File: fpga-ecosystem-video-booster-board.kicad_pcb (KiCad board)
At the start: 4 copper layers, 26.9 x 20.3 mm, 50 parts, among them J1 0473460001, J2 HDMI-PE10-19-LF, J3 61300411121, J4 M20-9990246, J5 M20-9990246, J6 685119134923_, U1 LP2985-33DBVR, U2 EFM32HG309, U3 PTN3363

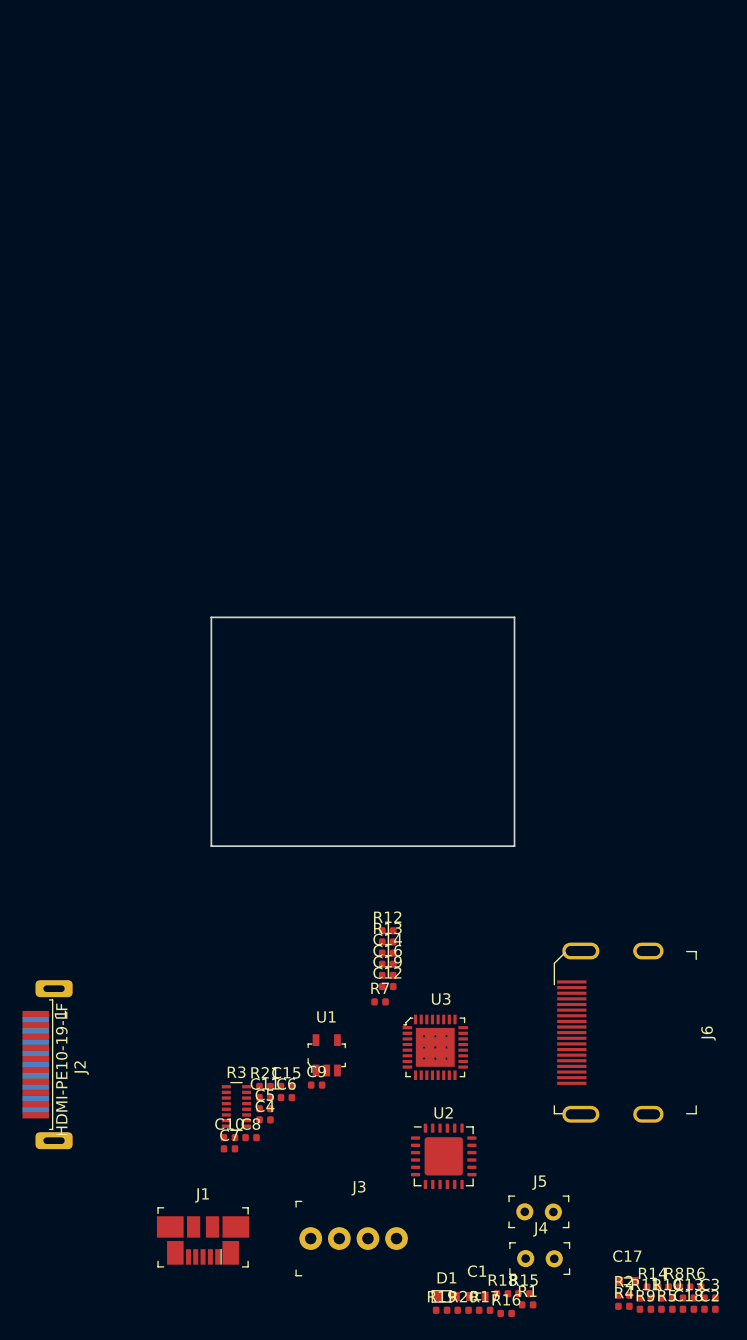
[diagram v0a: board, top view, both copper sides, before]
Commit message: Board shape, initial component layout
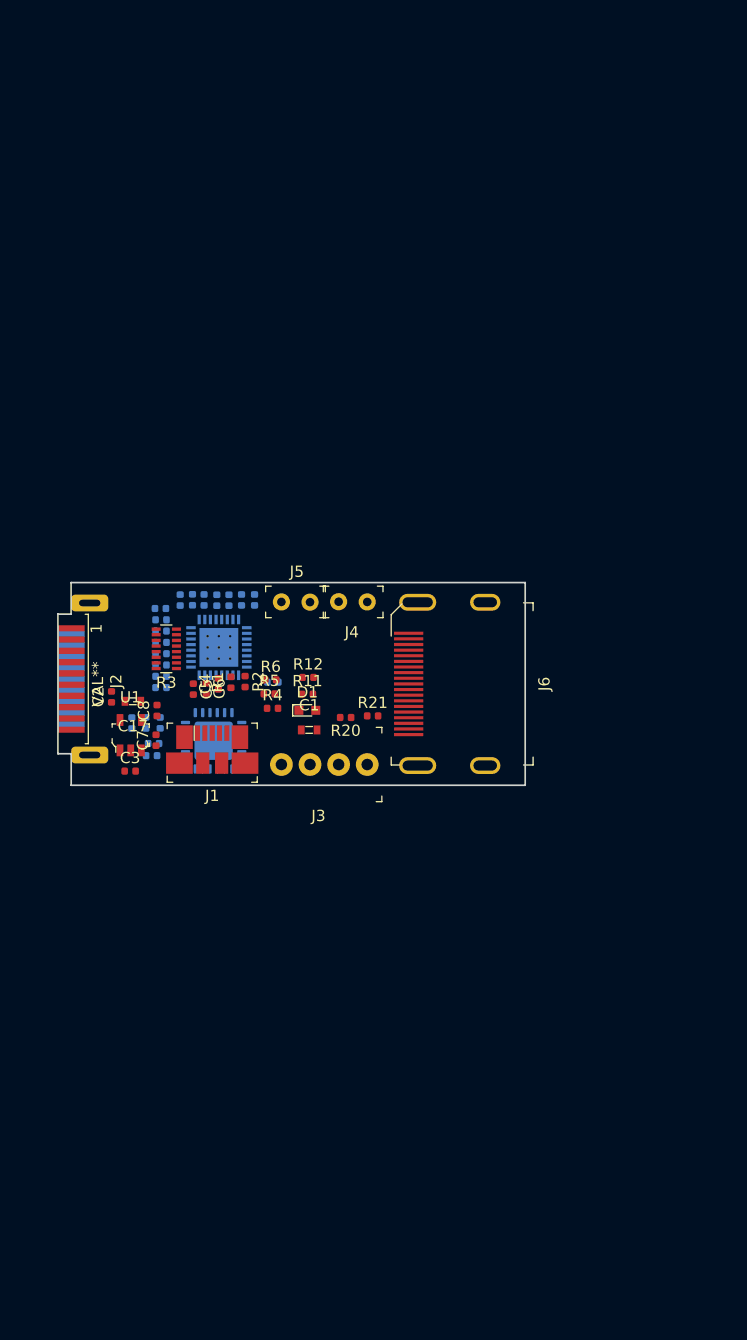
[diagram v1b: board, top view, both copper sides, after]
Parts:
- C10, C11, C12, C13, C14, C15, C16, C18, C19, C9, R10, R13, R14, R15, R16, R17, R18, R19, R7, R8, R9, U2, U3: moved to B.Cu
- J2: value HDMI-PE10-19-LF -> VAL**
- moved C18 77.5 mm to (124.4, 83.6), turned to 270 degrees
- moved C13 77.1 mm to (122.6, 84.3), turned to 180 degrees
- moved C2 76.0 mm to (118.3, 92.2), turned to 90 degrees
- moved R8 74.5 mm to (125.5, 83.5), turned to 270 degrees
- moved C3 69.6 mm to (119.9, 98.7)
- moved R15 67.8 mm to (126.5, 83.5), turned to 270 degrees
- moved C17 67.7 mm to (120.2, 92.5), turned to 180 degrees
- moved R10 67.1 mm to (122.0, 96.3)
- moved R14 66.5 mm to (122.6, 94.5), turned to 90 degrees
- moved R18 66.2 mm to (128.7, 83.6), turned to 270 degrees
- moved R9 65.9 mm to (121.8, 97.4)
- moved R6 65.8 mm to (132.4, 90.6)
- moved R19 65.5 mm to (129.8, 83.5), turned to 270 degrees
- moved R5 65.1 mm to (132.3, 91.9)
- moved R2 64.0 mm to (130.1, 90.8), turned to 270 degrees
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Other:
- board size 26.9 x 20.3 mm -> 41.5 x 18 mm

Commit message: New board shape, initial placement
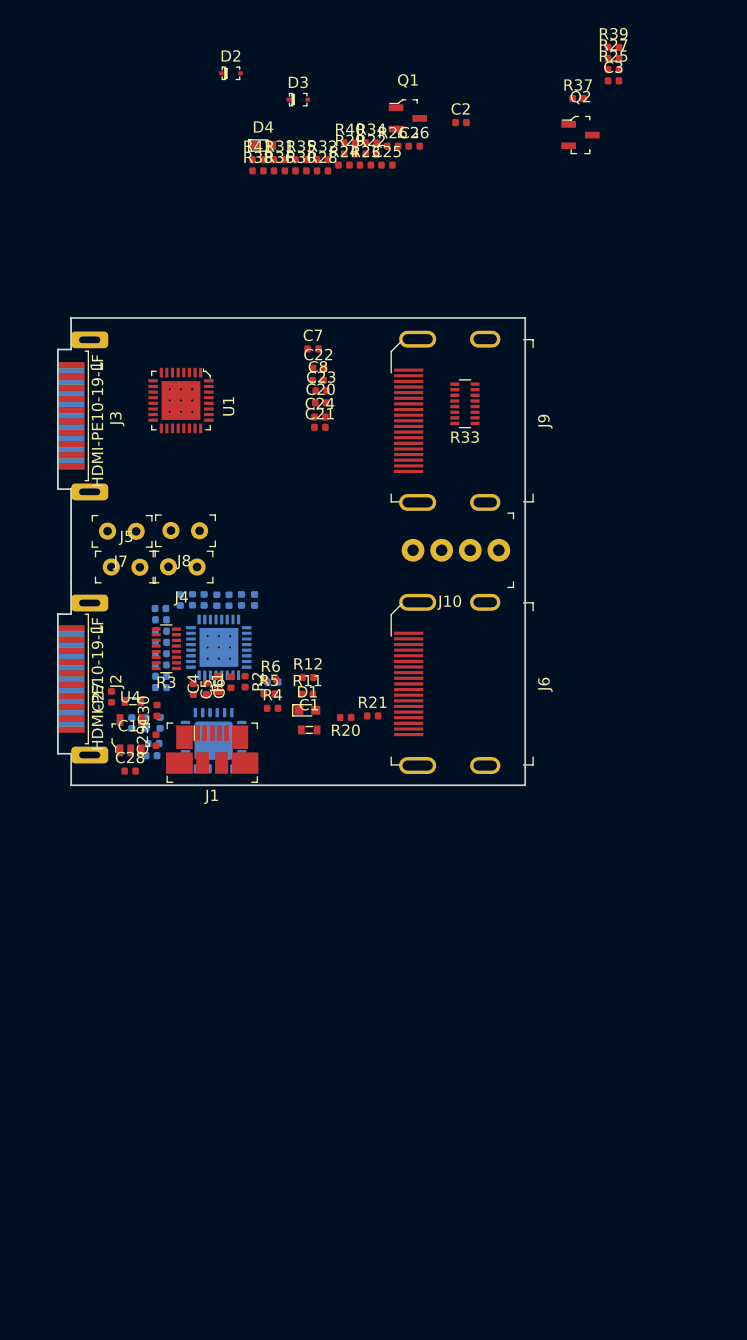
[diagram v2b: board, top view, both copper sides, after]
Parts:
- added C2: C_100n_0402_6V3, antmicro-footprints:0402-cap, F.Cu at (149.3, 41.1)
- added C20: C_100n_0402_6V3, antmicro-footprints:0402-cap, F.Cu at (136.8, 66.0)
- added C21: C_100n_0402_6V3, antmicro-footprints:0402-cap, F.Cu at (136.8, 68.2)
- added C22: C_100n_0402_6V3, antmicro-footprints:0402-cap, F.Cu at (136.6, 63.0)
- added C23: C_100n_0402_6V3, antmicro-footprints:0402-cap, F.Cu at (136.9, 65.0)
- added C24: C_100n_0402_6V3, antmicro-footprints:0402-cap, F.Cu at (136.8, 67.3)
- added C25: C_100n_0402_6V3, antmicro-footprints:0402-cap, F.Cu at (142.7, 44.9)
- added C26: C_1u_0402, antmicro-footprints:0402-cap, F.Cu at (145.1, 43.2)
- added C3: C_100n_0402_6V3, antmicro-footprints:0402-cap, F.Cu at (162.8, 37.4)
- added C7: C_100n_0402_6V3, antmicro-footprints:0402-cap, F.Cu at (136.2, 61.2)
- added C8: C_100n_0402_6V3, antmicro-footprints:0402-cap, F.Cu at (136.6, 64.0)
- added D2: BAT54-02V-V-G, antmicro-footprints:SOD-523, F.Cu at (128.9, 36.8)
- added D3: BAT54-02V-V-G, antmicro-footprints:SOD-523, F.Cu at (134.8, 39.1)
- added D4: LG_L29K-G2J1-24-Z, antmicro-footprints:LED_0603, F.Cu at (131.7, 43.2)
- added J3: HDMI-PE10-19-LF, antmicro-footprints:HDMI-PE10-19-LF, F.Cu at (114.7, 67.2)
- added J7: M20-9990246, antmicro-footprints:PinHeader_1x2_P2.54mm, F.Cu at (120.5, 77.5)
- added J8: M20-9990246, antmicro-footprints:PinHeader_1x2_P2.54mm, F.Cu at (126.1, 77.4)
- added J9: 685119134923_, antmicro-footprints:HDMI_A_Female_685119134923, F.Cu at (145.9, 67.6)
- added Q1: BSS138-7-F, antmicro-footprints:SOT-23-3, F.Cu at (144.6, 40.8)
- added Q2: BSS138-7-F, antmicro-footprints:SOT-23-3, F.Cu at (159.9, 42.3)
- added R22: R_10k_0402, antmicro-footprints:0402-res, F.Cu at (141.3, 43.9)
- added R23: R_10k_0402, antmicro-footprints:0402-res, F.Cu at (140.8, 44.9)
- added R24: R_100k_0402, antmicro-footprints:0402-res, F.Cu at (138.9, 44.9)
- added R25: R_100k_0402, antmicro-footprints:0402-res, F.Cu at (162.8, 36.4)
- added R26: R_10k_0402, antmicro-footprints:0402-res, F.Cu at (143.2, 43.2)
- added R27: R_10k_0402, antmicro-footprints:0402-res, F.Cu at (162.8, 35.5)
- added R28: R_10k_0402, antmicro-footprints:0402-res, F.Cu at (137.0, 45.4)
- added R29: R_10k_0402, antmicro-footprints:0402-res, F.Cu at (139.4, 43.9)
- added R30: R_10k_0402, antmicro-footprints:0402-res, F.Cu at (135.1, 45.4)
- added R31: R_10k_0402, antmicro-footprints:0402-res, F.Cu at (133.2, 44.4)
- added R32: R_10k_0402, antmicro-footprints:0402-res, F.Cu at (137.0, 44.4)
- added R33: 8x51R_0602_array, antmicro-footprints:R_Array_Convex_8x0602, F.Cu at (149.7, 66.1)
- added R34: R_10k_0402, antmicro-footprints:0402-res, F.Cu at (141.3, 42.9)
- added R35: R_10k_0402, antmicro-footprints:0402-res, F.Cu at (135.1, 44.4)
- added R36: R_10k_0402, antmicro-footprints:0402-res, F.Cu at (133.2, 45.4)
- added R37: R_10k_0402, antmicro-footprints:0402-res, F.Cu at (159.7, 39.0)
- added R38: R_10k_0402, antmicro-footprints:0402-res, F.Cu at (131.3, 45.4)
- added R39: R_10k_0402, antmicro-footprints:0402-res, F.Cu at (162.8, 34.5)
- added R40: R_10k_0402, antmicro-footprints:0402-res, F.Cu at (139.4, 42.9)
- added R41: R_330R_0402, antmicro-footprints:0402-res, F.Cu at (131.3, 44.4)
- added U1: PTN3363, antmicro-footprints:QFN-32-1EP_5x5mm, F.Cu at (124.0, 66.3)
- C4: value C_1u_0402 -> C_10u_0603; footprint antmicro-footprints:0402-cap -> antmicro-footprints:0603-cap
- J2: value VAL** -> HDMI-PE10-19-LF
- R11, R12: value R_15R_0402 -> R_0R_0402
- R14, R15, R5, R6: value R_10k_0402 -> R_100k_0402
- R17: value R_10k_0402 -> R_12k4_0402
- R18, R21: value R_4k7_0402 -> R_10k_0402
- R19, R20: value R_4k7_0402 -> R_100k_0402
- R7, R8: value R_100k_0402 -> R_0R_0402
- moved J10 22.3 mm to (152.7, 79.1)
- moved J4 15.4 mm to (125.9, 80.6)
- moved J5 15.4 mm to (118.2, 80.6)
- renumbered C2 to C27, C3 to C28, C7 to C29, C8 to C30, J3 to J10, U1 to U4
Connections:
- net /CEC renamed /TX_CEC
- net /C_IN_CLK_N renamed /C_TX_IN_CLK_N
- net /C_IN_CLK_P renamed /C_TX_IN_CLK_P
- net /C_IN_D0_N renamed /C_TX_IN_D0_N
- net /C_IN_D0_P renamed /C_TX_IN_D0_P
- net /C_IN_D1_N renamed /C_TX_IN_D1_N
- net /C_IN_D1_P renamed /C_TX_IN_D1_P
- net /C_IN_D2_N renamed /C_TX_IN_D2_N
- net /C_IN_D2_P renamed /C_TX_IN_D2_P
- net /IN_CLK_P renamed /TX_IN_CLK_P
- net /IN_D0_N renamed /TX_IN_D0_N
- net /IN_D0_P renamed /TX_IN_D0_P
- net /IN_D1_N renamed /TX_IN_D1_N
- net /IN_D1_P renamed /TX_IN_D1_P
- net /IN_D2_N renamed /TX_IN_D2_N
- net /IN_D2_P renamed /TX_IN_D2_P
- net /OUT_CLK_N renamed /TX_OUT_CLK_N
- net /OUT_CLK_P renamed /TX_OUT_CLK_P
- net /OUT_D0_N renamed /TX_OUT_D0_N
- net /OUT_D0_P renamed /TX_OUT_D0_P
- net /OUT_D1_N renamed /TX_OUT_D1_N
- net /OUT_D1_P renamed /TX_OUT_D1_P
- net /OUT_D2_N renamed /TX_OUT_D2_N
- net /OUT_D2_P renamed /TX_OUT_D2_P
- net /UTILITY renamed /TX_UTILITY
- C12 pad 2: /IN_CLK_N -> Net-(C12-Pad2)
- C4 pad 1: Net-(C4-Pad1) -> VDD
- J2 pad 12: /IN_CLK_N -> /TX_IN_CLK_N
- J2 pad 15: /SCL_SRC -> Net-(J2-Pad15)
- J2 pad 16: /SDA_SRC -> Net-(J2-Pad16)
- J2 pad 18: +5V -> /TX_5V
- J2 pad 19: /HPD_SRC -> /TX_HPD
- J4 pad 1: /EQ0 -> /TX_EQ0
- J5 pad 1: /EQ1 -> /TX_EQ1
- J6 pad 15: /SCL_SINK -> /TX_SCL
- J6 pad 16: /SDA_SINK -> /TX_SDA
- J6 pad 18: +5V -> /TX_5V
- J6 pad 19: /HPD_SINK -> /TX_HPD
- R10 pad 1: /DBG_SWDIO -> /TX_EQ1
- R10 pad 2: /UART_RX -> Net-(R10-Pad2)
- R11 pad 1: /SCL_MCU -> Net-(J3-Pad15)
- R11 pad 2: /SCL_SRC -> /TX_SDA
- R12 pad 1: /SDA_MCU -> Net-(J3-Pad16)
- R12 pad 2: /SDA_SRC -> /TX_SCL
- R14 pad 2: /DCC_EN -> /RX_EQ0
- R15 pad 2: /DDET -> /RX_EQ1
- R16 pad 1: VDD -> GND
- R16 pad 2: /HIZ_EN -> /RX_5V
- R17 pad 1: /HIZ_EN -> GND
- R17 pad 2: GND -> Net-(R17-Pad2)
- R18 pad 1: VDD -> Net-(Q1-Pad3)
- R18 pad 2: /SDA_SRC -> VDD
- R19 pad 2: /SCL_SRC -> /TX_DCC_EN
- R20 pad 1: +5V -> /TX_DCC_EN
- R20 pad 2: /SDA_SINK -> GND
- R21 pad 1: +5V -> VDD
- R21 pad 2: /SCL_SINK -> /TX_DDET
- R3 pad 16: /IN_CLK_N -> Net-(C12-Pad2)
- R5 pad 1: /EQ0 -> VDD
- R5 pad 2: Net-(R5-Pad2) -> /TX_EQ0
- R6 pad 1: /EQ1 -> VDD
- R6 pad 2: Net-(R6-Pad2) -> /TX_EQ1
- R7 pad 1: VDD -> Net-(J2-Pad15)
- R7 pad 2: /EQ0 -> /TX_SDA
- R8 pad 1: VDD -> Net-(J2-Pad16)
- R8 pad 2: /EQ1 -> /TX_SCL
- R9 pad 1: /DBG_SWCLK -> /TX_EQ0
- R9 pad 2: /UART_TX -> Net-(R9-Pad2)
- U2 pad 10: /UART_TX -> /TX_HIZ_EN
- U2 pad 11: /UART_RX -> /RX_HIZ_EN
- U2 pad 16: Net-(C4-Pad1) -> Net-(C26-Pad1)
- U2 pad 21: (no net) -> Net-(R41-Pad1)
- U2 pad 23: /SDA_MCU -> /MCU_SDA
- U2 pad 24: /SCL_MCU -> /MCU_SCL
- U2 pad 3: /DDET -> Net-(R39-Pad2)
- U2 pad 4: /DCC_EN -> Net-(R40-Pad2)
- U2 pad 5: Net-(R5-Pad2) -> Net-(R9-Pad2)
- U2 pad 6: Net-(R6-Pad2) -> Net-(R10-Pad2)
- U2 pad 8: /HIZ_EN -> Net-(R38-Pad2)
- U3 pad 17: GND -> Net-(Q2-Pad3)
- U3 pad 19: /SCL_SINK -> /TX_SDA
- U3 pad 2: /EQ1 -> /TX_EQ1
- U3 pad 20: /SDA_SINK -> /TX_SCl
- U3 pad 21: /HPD_SINK -> Net-(U3-Pad21)
- U3 pad 22: /DCC_EN -> /TX_DCC_EN
- U3 pad 24: /HIZ_EN -> /TX_HIZ_EN
- U3 pad 3: /DDET -> /TX_DDET
- U3 pad 5: /HPD_SRC -> Net-(U3-Pad5)
- U3 pad 6: /SDA_SRC -> /MCU_SDA
- U3 pad 7: /SCL_SRC -> /MCU_SCL
- U3 pad 8: /EQ0 -> /TX_EQ0
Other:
- board size 41.5 x 18 mm -> 41.5 x 41.5 mm

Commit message: Channels flipped for 1-side component placement
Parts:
- added R42: R_49R9_0402, antmicro-footprints:0402-res, F.Cu at (118.3, 88.4)
- added R43: R_49R9_0402, antmicro-footprints:0402-res, F.Cu at (118.3, 87.4)
- added R44: R_49R9_0402, antmicro-footprints:0402-res, F.Cu at (118.3, 90.4)
- added R45: R_49R9_0402, antmicro-footprints:0402-res, F.Cu at (118.3, 89.4)
- added R46: R_49R9_0402, antmicro-footprints:0402-res, F.Cu at (118.3, 92.4)
- added R47: R_49R9_0402, antmicro-footprints:0402-res, F.Cu at (118.3, 91.4)
- added R48: R_49R9_0402, antmicro-footprints:0402-res, F.Cu at (131.0, 69.5)
- added R49: R_49R9_0402, antmicro-footprints:0402-res, F.Cu at (132.0, 67.9)
- added R50: R_49R9_0402, antmicro-footprints:0402-res, F.Cu at (130.0, 67.4)
- added R51: R_49R9_0402, antmicro-footprints:0402-res, F.Cu at (130.1, 65.9)
- added R52: R_49R9_0402, antmicro-footprints:0402-res, F.Cu at (132.0, 65.4)
- added R53: R_49R9_0402, antmicro-footprints:0402-res, F.Cu at (132.0, 63.8)
- added R54: R_49R9_0402, antmicro-footprints:0402-res, F.Cu at (130.0, 63.4)
- added R55: R_49R9_0402, antmicro-footprints:0402-res, F.Cu at (130.0, 61.8)
- C10, C11, C12, C13, C14, C15, C16, C18, C9, R10, R13, R14, R15, R16, R17, R18, R19, R7, R8, R9, U2, U3: moved to F.Cu
- R3, R33: value 8x51R_0602_array -> R_49R9_0402; footprint antmicro-footprints:R_Array_Convex_8x0602 -> antmicro-footprints:0402-res
- moved R39 77.9 mm to (126.7, 103.5), turned to 270 degrees
- moved D4 69.3 mm to (138.1, 112.2)
- moved R41 67.4 mm to (134.9, 111.8)
- moved R27 58.0 mm to (129.2, 82.7), turned to 90 degrees
- moved R25 52.2 mm to (123.5, 70.8), turned to 270 degrees
- moved Q2 46.3 mm to (131.2, 78.6)
- moved C27 46.0 mm to (163.6, 84.2), turned to 180 degrees
- moved C29 45.3 mm to (163.7, 77.9)
- moved C3 45.0 mm to (124.4, 60.8), turned to 270 degrees
- moved U4 45.0 mm to (162.6, 81.2)
- moved C28 43.9 mm to (161.3, 84.2), turned to 180 degrees
- moved C30 42.3 mm to (161.7, 78.0)
- moved R38 38.6 mm to (137.8, 83.5)
- moved R33 36.8 mm to (118.3, 85.4), turned to 0 degrees
- moved R17 33.8 mm to (123.0, 60.8)
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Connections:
- C10 pad 1: /C_TX_IN_D1_N -> /C_TX_IN_D0_N
- C10 pad 2: /TX_IN_D1_N -> /TX_IN_D0_N
- C11 pad 1: /C_TX_IN_D0_N -> /C_TX_IN_D1_N
- C11 pad 2: /TX_IN_D0_N -> /TX_IN_D1_N
- C12 pad 1: /C_TX_IN_CLK_N -> /C_TX_IN_D2_N
- C12 pad 2: Net-(C12-Pad2) -> /TX_IN_D2_N
- C13 pad 1: /C_TX_IN_D2_P -> /C_TX_IN_CLK_P
- C13 pad 2: /TX_IN_D2_P -> /TX_IN_CLK_P
- C14 pad 1: /C_TX_IN_D1_P -> /C_TX_IN_D0_P
- C14 pad 2: /TX_IN_D1_P -> /TX_IN_D0_P
- C15 pad 1: /C_TX_IN_D0_P -> /C_TX_IN_D1_P
- C15 pad 2: /TX_IN_D0_P -> /TX_IN_D1_P
- C16 pad 1: /C_TX_IN_CLK_P -> /C_TX_IN_D2_P
- C16 pad 2: /TX_IN_CLK_P -> /TX_IN_D2_P
- C9 pad 1: /C_TX_IN_D2_N -> /C_TX_IN_CLK_N
- C9 pad 2: /TX_IN_D2_N -> /TX_IN_CLK_N
- D2 pad A: (no net) -> /TX_5V
- D2 pad K: (no net) -> +5V
- D3 pad A: (no net) -> /RX_5V
- D3 pad K: (no net) -> +5V
- R3 pad 2: VDD -> /TX_IN_D2_P
- R33 pad 2: VDD -> /TX_IN_D2_N
- U3 pad 10: /TX_OUT_D2_N -> /TX_OUT_CLK_N
- U3 pad 11: /TX_OUT_D1_P -> /TX_OUT_D0_P
- U3 pad 12: /TX_OUT_D1_N -> /TX_OUT_D0_N
- U3 pad 13: /TX_OUT_D0_P -> /TX_OUT_D1_P
- U3 pad 14: /TX_OUT_D0_N -> /TX_OUT_D1_N
- U3 pad 15: /TX_OUT_CLK_P -> /TX_OUT_D2_P
- U3 pad 16: /TX_OUT_CLK_N -> /TX_OUT_D2_N
- U3 pad 25: /C_TX_IN_CLK_N -> /C_TX_IN_D2_N
- U3 pad 26: /C_TX_IN_CLK_P -> /C_TX_IN_D2_P
- U3 pad 27: /C_TX_IN_D0_N -> /C_TX_IN_D1_N
- U3 pad 28: /C_TX_IN_D0_P -> /C_TX_IN_D1_P
- U3 pad 29: /C_TX_IN_D1_N -> /C_TX_IN_D0_N
- U3 pad 30: /C_TX_IN_D1_P -> /C_TX_IN_D0_P
- U3 pad 31: /C_TX_IN_D2_N -> /C_TX_IN_CLK_N
- U3 pad 32: /C_TX_IN_D2_P -> /C_TX_IN_CLK_P
- U3 pad 9: /TX_OUT_D2_P -> /TX_OUT_CLK_P
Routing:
- net /RX_IN_D1_P: track 0.00 -> 5.54 mm
- net /TX_IN_D1_P: track 0.00 -> 5.44 mm, vias 0 -> 1
- net /TX_IN_D1_N: track 0.00 -> 5.42 mm, vias 0 -> 1
- net /RX_IN_D1_N: track 0.00 -> 5.40 mm
- net /RX_IN_CLK_N: track 0.00 -> 5.36 mm
- net /TX_IN_D2_N: track 0.00 -> 5.35 mm, vias 0 -> 2
- net /RX_IN_CLK_P: track 0.00 -> 5.21 mm
- net /TX_IN_CLK_P: track 0.00 -> 5.21 mm, vias 0 -> 1
- net /TX_IN_D0_P: track 0.00 -> 5.02 mm, vias 0 -> 2
- net /TX_IN_D2_P: track 0.00 -> 5.01 mm, vias 0 -> 2
- net /TX_IN_CLK_N: track 0.00 -> 4.96 mm, vias 0 -> 1
- net /TX_IN_D0_N: track 0.00 -> 4.93 mm, vias 0 -> 2
- net /RX_IN_D2_N: track 0.00 -> 4.91 mm
- net /RX_IN_D2_P: track 0.00 -> 4.76 mm
- net /RX_IN_D0_P: track 0.00 -> 4.33 mm
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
